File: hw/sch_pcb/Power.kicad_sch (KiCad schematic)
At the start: 45 parts, among them J3 HEADER_1x02, U11 LTC3601, U9 LTC3601

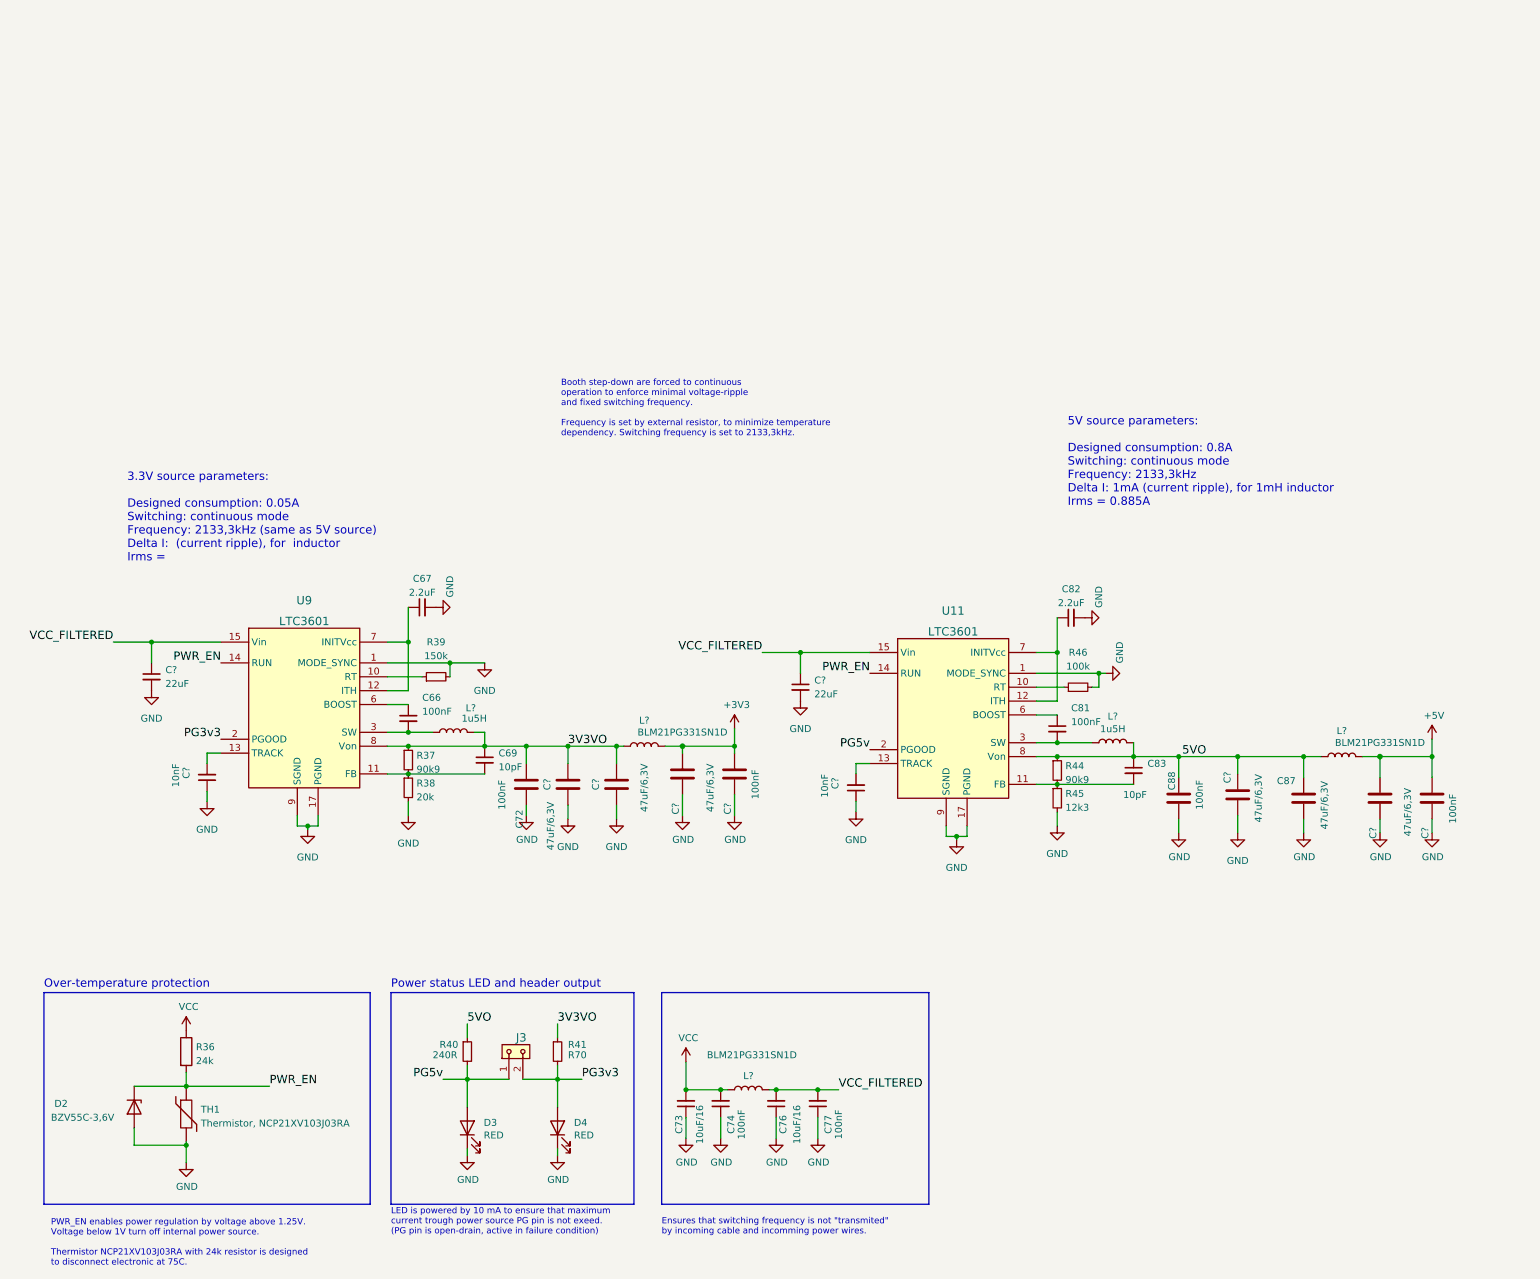
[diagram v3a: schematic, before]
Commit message: Define footprints of new components and update PCB.
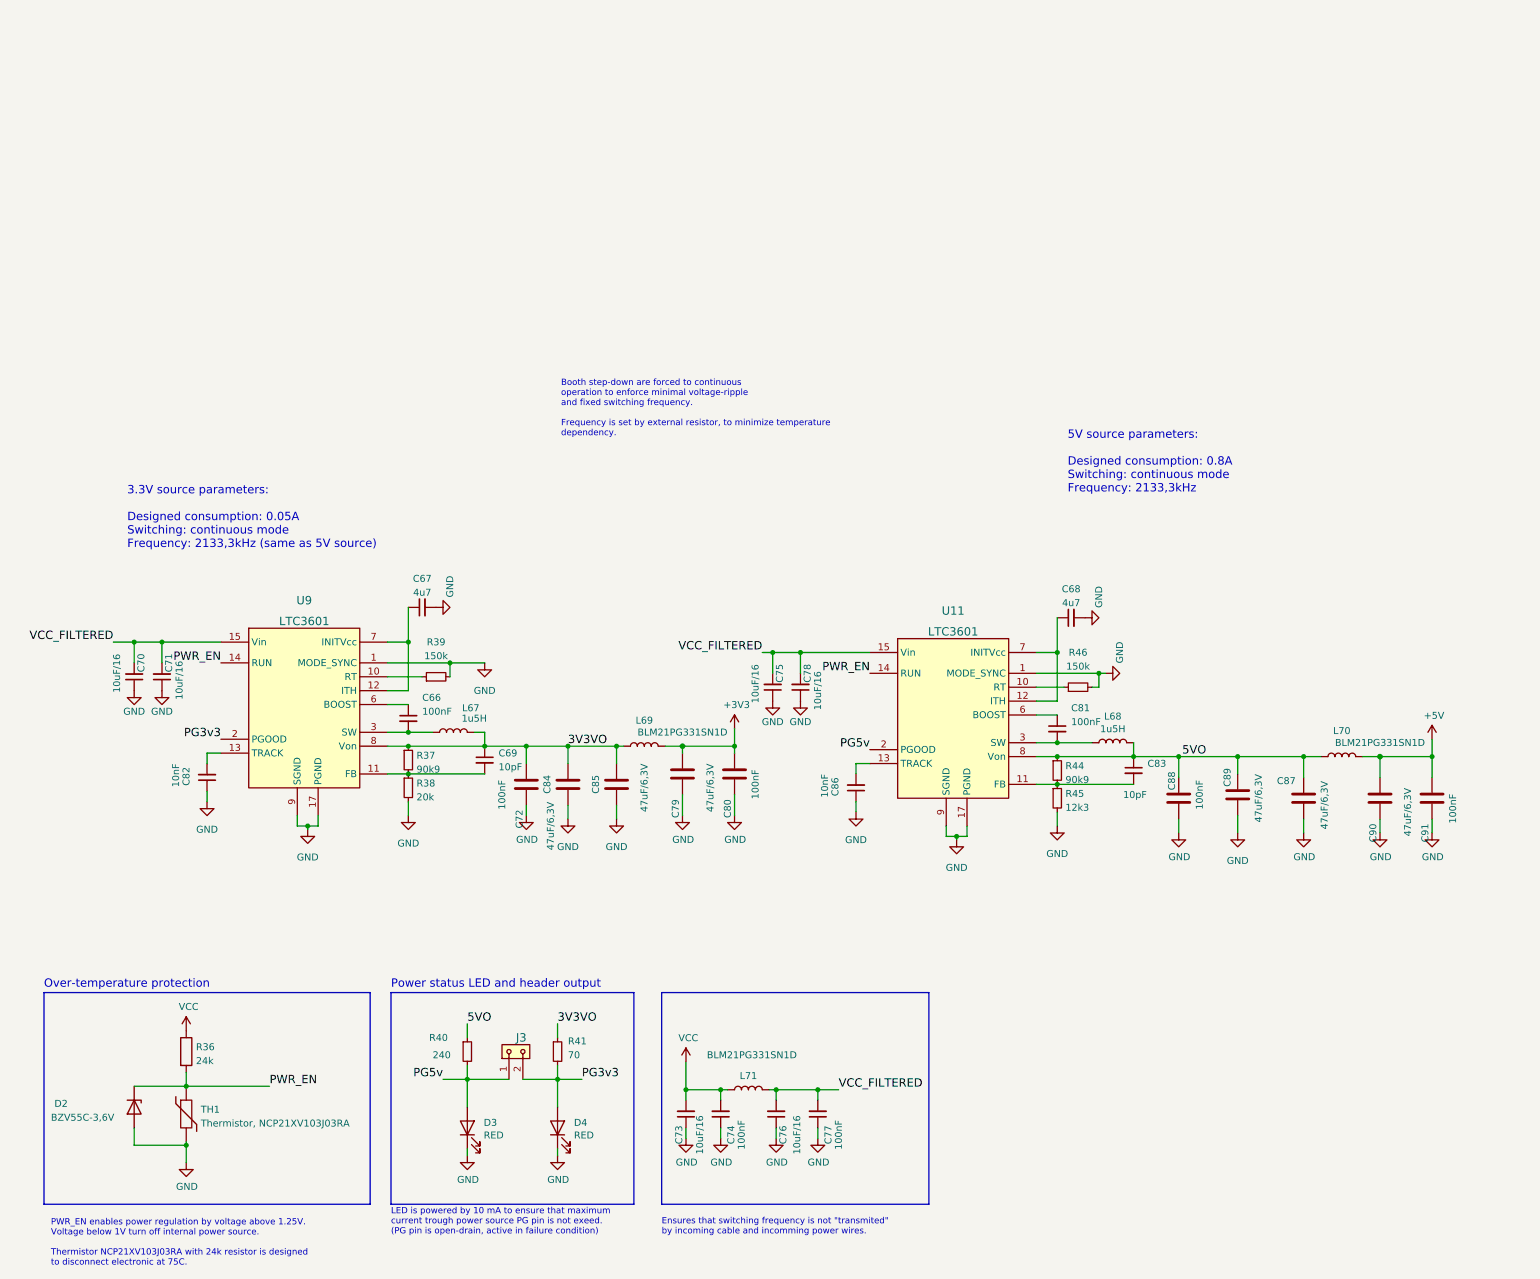
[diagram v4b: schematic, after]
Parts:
- removed C82: 2.2uF, symbol Device:C_Small
- removed C? (x2): 22uF, symbol Device:C_Small
- added C68: 4u7, Capacitor_SMD:C_0603_1608Metric, symbol Device:C_Small
- added C70, C71, C75, C78: 10uF/16, Capacitor_SMD:C_0805_2012Metric, symbol Device:C_Small
- C66: value 0.1uF -> 100nF; footprint (none) -> Capacitor_SMD:C_0603_1608Metric; UST_ID (none) -> 5c70984812875079b91f8bf2
- C67: value 0.1uF -> 4u7; footprint (none) -> Capacitor_SMD:C_0603_1608Metric; UST_ID (none) -> 5e3ff54b1287502a33bad705
- C69, C83: footprint (none) -> Capacitor_SMD:C_0603_1608Metric; UST_ID (none) -> 5c70984812875079b91f8be2
- C81: footprint (none) -> Capacitor_SMD:C_0603_1608Metric; UST_ID (none) -> 5c70984812875079b91f8bf2
- D2: UST_ID (none) -> 5c70984512875079b91f88b1
- R36: footprint Resistor_SMD:R_0805_2012Metric -> Resistor_SMD:R_0603_1608Metric; UST_ID (none) -> 5c70984512875079b91f8965
- R37: value 180k -> 90k9
- R38: value 40k -> 20k
- R39: footprint (none) -> Resistor_SMD:R_0603_1608Metric
- R40: value 1k -> 240; UST_ID (none) -> 60d337a4128750016518cb3a
- R41: value 1k -> 70
- R46: value 100k -> 150k; footprint (none) -> Resistor_SMD:R_0603_1608Metric
- TH1: UST_ID (none) -> 5c70984712875079b91f8ac5
- gave numbers to parts that had none: 14
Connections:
- net GND: now also C68.2, C70.1, C71.1, C75.1, C78.1
- net VCC_FILTERED: now also C70.2, C71.2, C75.2, C78.2
- net at U11.12 (ITH), U11.7 (INITVcc): now also C68.1
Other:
- note added: "3.3V source parameters: Designed consumption: 0.05A Switching: continuous mode Frequency: 2133,3kHz (same as 5V source)"
- note added: "5V source parameters: Designed consumption: 0.8A Switching: continuous mode Frequency: 2133,3kHz"
- note added: "Booth step-down are forced to continuous operation to enforce minimal voltage-ripple and fixed switching frequency. Frequency is set by external resistor, to minimize temperature dependency."
- note removed: "3.3V source parameters: Designed consumption: 0.05A Switching: continuous mode Frequency: 2133,3kHz (same as 5V source) Delta I: (current ripple), for inductor Irms ="
- note removed: "5V source parameters: Designed consumption: 0.8A Switching: continuous mode Frequency: 2133,3kHz Delta I: 1mA (current ripple), for 1mH inductor Irms = 0.885A"
- note removed: "Booth step-down are forced to continuous operation to enforce minimal voltage-ripple and fixed switching frequency. Frequency is set by external resistor, to minimize temperature dependency. Switching frequency is set to 2133,3kHz."
- moved on the sheet: C73, C74, C76, C77

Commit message: Grouping components according to function.
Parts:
- added C26: 10uF/16, Capacitor_SMD:C_0805_2012Metric, symbol QFHMIX01C-rescue:C_Small-device-QFHMIX01B-rescue
- added C27: 100nF, Capacitor_SMD:C_0603_1608Metric, symbol QFHMIX01C-rescue:C_Small-device-QFHMIX01B-rescue
- added D1: M4, Diode_SMD:D_SMA, symbol QFHMIX01C-rescue:D_Small-device-QFHMIX01B-rescue
- added J2: +12V, Mlab_Pin_Headers:Straight_2x03, symbol QFHMIX01C-rescue:HEADER_2x03_PARALLEL-MLAB_HEADER
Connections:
- net 3V3VO is gone; now on net +3V3: C69.1, C72.2, C84.2, C85.2, L67.2, L69.1, R37.1, R41.1, U9.8 (Von)
- net +3V3: no longer C79.2, C80.2, L69.2
- net GND: now also C26.2, C27.2, D1.2 (A), J2.1, J2.2, J2.5, J2.6
- net VCC: now also C26.1, C27.1, D1.1 (K), J2.3, J2.4
- new net +3.3VA: C79.2, C80.2, L69.2
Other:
- note added: "Alternative power input"

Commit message: All components placed in PCB layout.
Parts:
- removed J3: HEADER_1x02, Mlab_Pin_Headers:Straight_1x02, symbol MLAB_HEADER:HEADER_1x02
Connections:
- net VCC: no longer C26.1, C27.1, D1.1 (K), J2.3, J2.4
- net VCC_FILTERED renamed VDDA
- net VDDA: now also C26.1, C27.1, D1.1 (K), J2.3, J2.4
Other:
- moved on the sheet: C73, C74, C76, C77, L71

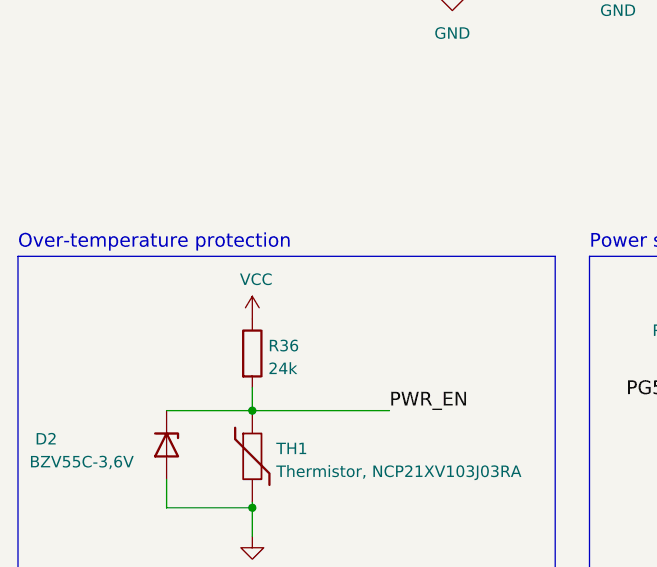
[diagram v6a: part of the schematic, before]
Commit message: Removed duplicite copper pour.
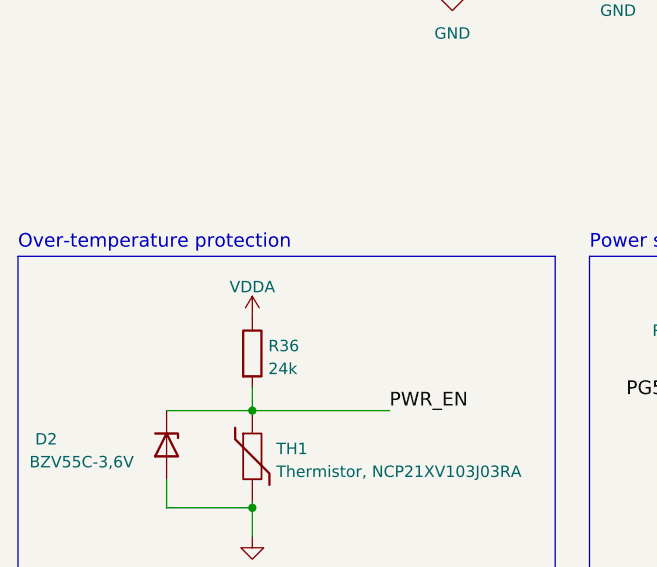
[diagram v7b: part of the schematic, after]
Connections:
- net VCC: no longer R36.1
- net VDDA: now also R36.1
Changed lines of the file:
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@@
     (pin "2")
-  )
-  (symbol (lib_id "power:VCC") (at 44.45 144.78 0) (unit 1)
-    (in_bom yes) (on_board yes)
-    (property "Reference" "#PWR058" (id 0) (at 44.45 148.59 0)
-      (effects (font (size 1.27 1.27)) hide)
-    )
-    (property "Value" "VCC" (id 1) (at 44.8818 140.3858 0))
-    (property "Footprint" "" (id 2) (at 44.45 144.78 0)
-      (effects (font (size 1.27 1.27)) hide)
-    )
-    (property "Datasheet" "" (id 3) (at 44.45 144.78 0)
-      (effects (font (size 1.27 1.27)) hide)
-    )
-    (pin "1")
   )
   (symbol (lib_id "power:GND") (at 99.06 77.47 0) (unit 1)
@@
       (effects (font (size 1.27 1.27)) hide)
     )
+    (pin "1")
+  )
+  (symbol (lib_id "Power_symbols:VDDA") (at 44.45 144.78 0) (unit 1)
+    (in_bom yes) (on_board yes) (fields_autoplaced)
+    (property "Reference" "#PWR?" (id 0) (at 44.45 148.59 0)
+      (effects (font (size 1.27 1.27)) hide)
+    )
+    (property "Value" "VDDA" (id 1) (at 44.45 141.2042 0))
+    (property "Footprint" "" (id 2) (at 44.45 144.78 0)
+      (effects (font (size 1.27 1.27)) hide)
+    )
+    (property "Datasheet" "" (id 3) (at 44.45 144.78 0)
+      (effects (font (size 1.27 1.27)) hide)
+    )

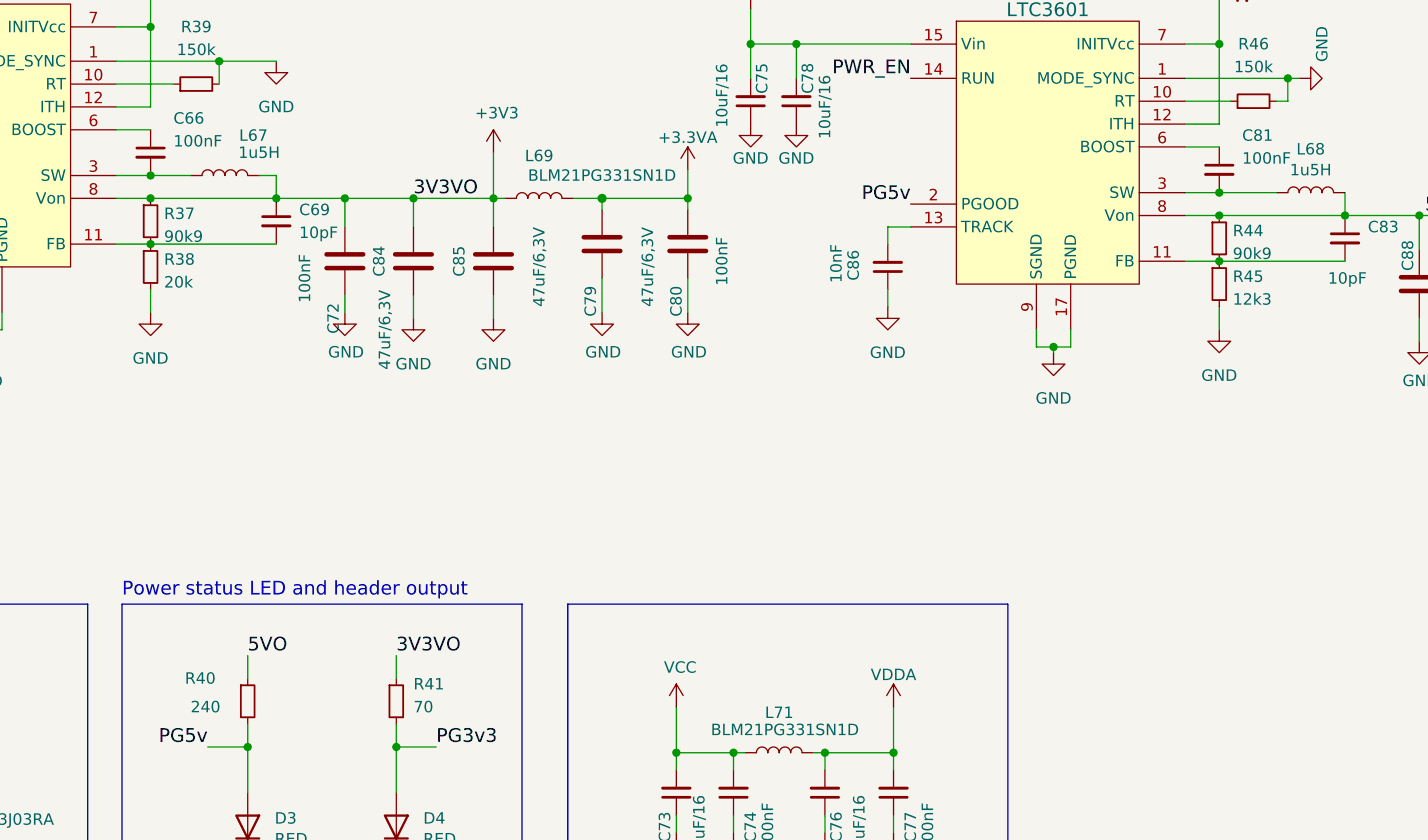
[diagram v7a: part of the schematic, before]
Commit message: The firts dirty layout of new switched power supplies.
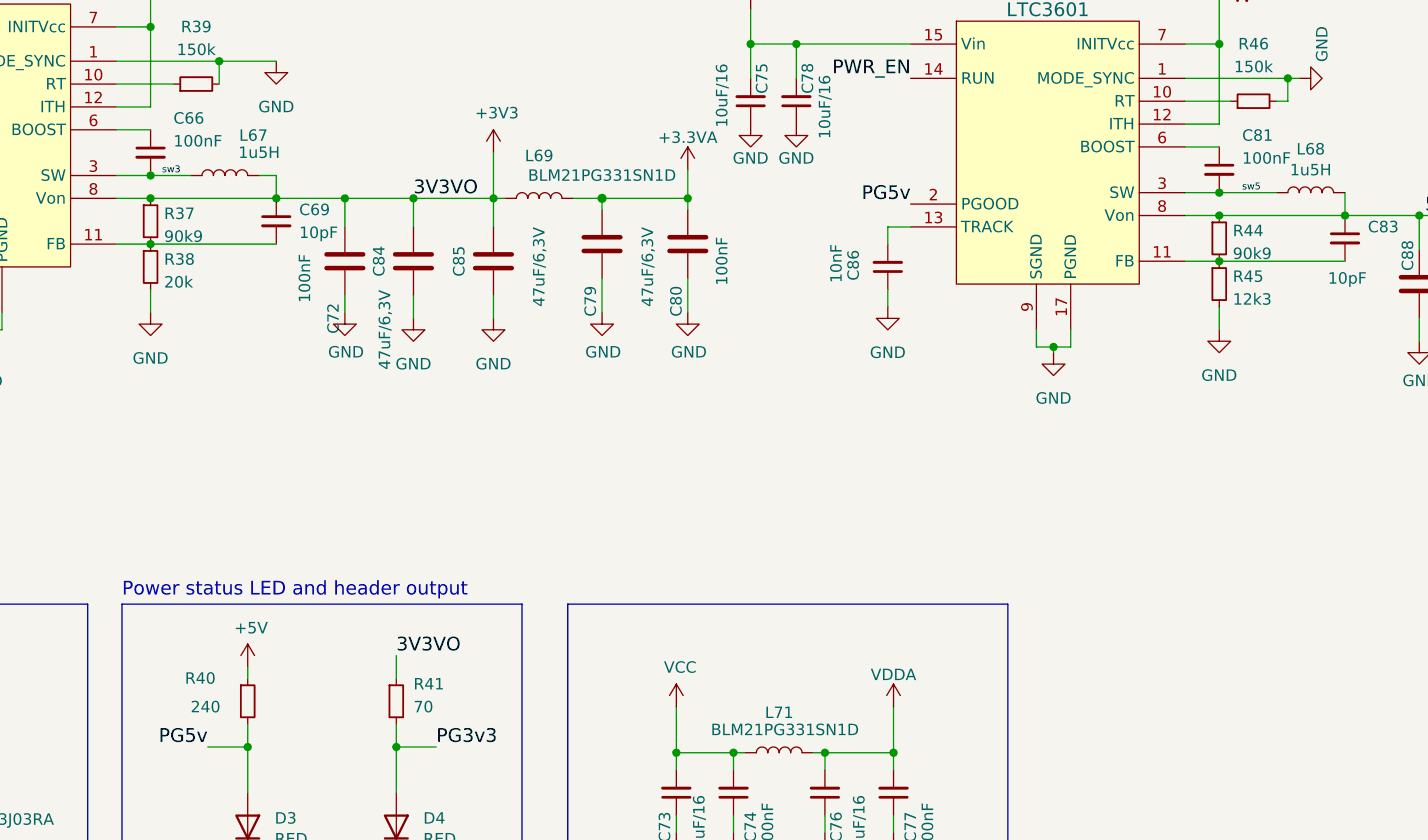
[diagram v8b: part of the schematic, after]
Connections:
- net +5V: now also R40.1
- net 5VO: no longer R40.1
- net sw3: now reaches C66.2, L67.1, U9.3 (SW), U9.4 (SW)
- net sw5: now reaches C81.2, L68.1, U11.3 (SW), U11.4 (SW)
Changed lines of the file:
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@@
     (stroke (width 0) (type solid) (color 0 0 0 0))
-  )
-  (wire (pts (xy 95.885 146.05) (xy 95.885 143.51))
-    (stroke (width 0) (type default) (color 0 0 0 0))
   )
   (wire (pts (xy 203.835 94.615) (xy 200.025 94.615))
@@
   )
   (wire (pts (xy 236.855 94.615) (xy 248.92 94.615))
+    (stroke (width 0) (type default) (color 0 0 0 0))
+  )
+  (wire (pts (xy 95.885 144.78) (xy 95.885 146.05))
     (stroke (width 0) (type default) (color 0 0 0 0))
   )
@@
     (effects (font (size 1.524 1.524)) (justify right bottom))
   )
+  (label "sw3" (at 86.36 90.17 0)
+    (effects (font (size 0.762 0.762)) (justify left bottom))
+  )
   (label "5VO" (at 226.695 94.615 0)
     (effects (font (size 1.524 1.524)) (justify left bottom))
   )
-  (label "5VO" (at 95.885 143.51 0)
-    (effects (font (size 1.524 1.524)) (justify left bottom))
-  )
   (label "PG5v" (at 91.44 153.67 180)
     (effects (font (size 1.524 1.524)) (justify right bottom))
@@
   (label "PG3v3" (at 50.8 91.44 180)
     (effects (font (size 1.524 1.524)) (justify right bottom))
+  )
+  (label "sw5" (at 206.375 92.075 0)
+    (effects (font (size 0.762 0.762)) (justify left bottom))
   )
   (symbol (lib_id "Device:L") (at 154.94 154.305 90) (unit 1)
@@
     (pin "9")
   )
+  (symbol (lib_id "power:+5V") (at 95.885 144.78 0) (unit 1)
+    (in_bom yes) (on_board yes)
+    (property "Reference" "#PWR?" (id 0) (at 95.885 148.59 0)
+      (effects (font (size 1.27 1.27)) hide)
+    )
+    (property "Value" "+5V" (id 1) (at 96.2533 140.4556 0))
+    (property "Footprint" "" (id 2) (at 95.885 144.78 0)
+      (effects (font (size 1.27 1.27)) hide)
+    )
+    (property "Datasheet" "" (id 3) (at 95.885 144.78 0)
+      (effects (font (size 1.27 1.27)) hide)
+    )
+    (pin "1")
+  )
   (symbol (lib_id "power:GND") (at 106.68 105.41 0) (unit 1)
     (in_bom yes) (on_board yes)
@@
   (symbol (lib_id "Power_symbols:VDDA") (at 44.45 144.78 0) (unit 1)
     (in_bom yes) (on_board yes) (fields_autoplaced)
-    (property "Reference" "#PWR?" (id 0) (at 44.45 148.59 0)
-      (effects (font (size 1.27 1.27)) hide)
-    )
+    (property "Reference" "#PWR0109" (id 0) (at 44.45 148.59 0)
+      (effects (font (size 1.27 1.27)) hide)
+    )
